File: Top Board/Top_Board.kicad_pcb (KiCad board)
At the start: 2 copper layers, 135.6 x 135.6 mm, 3 parts

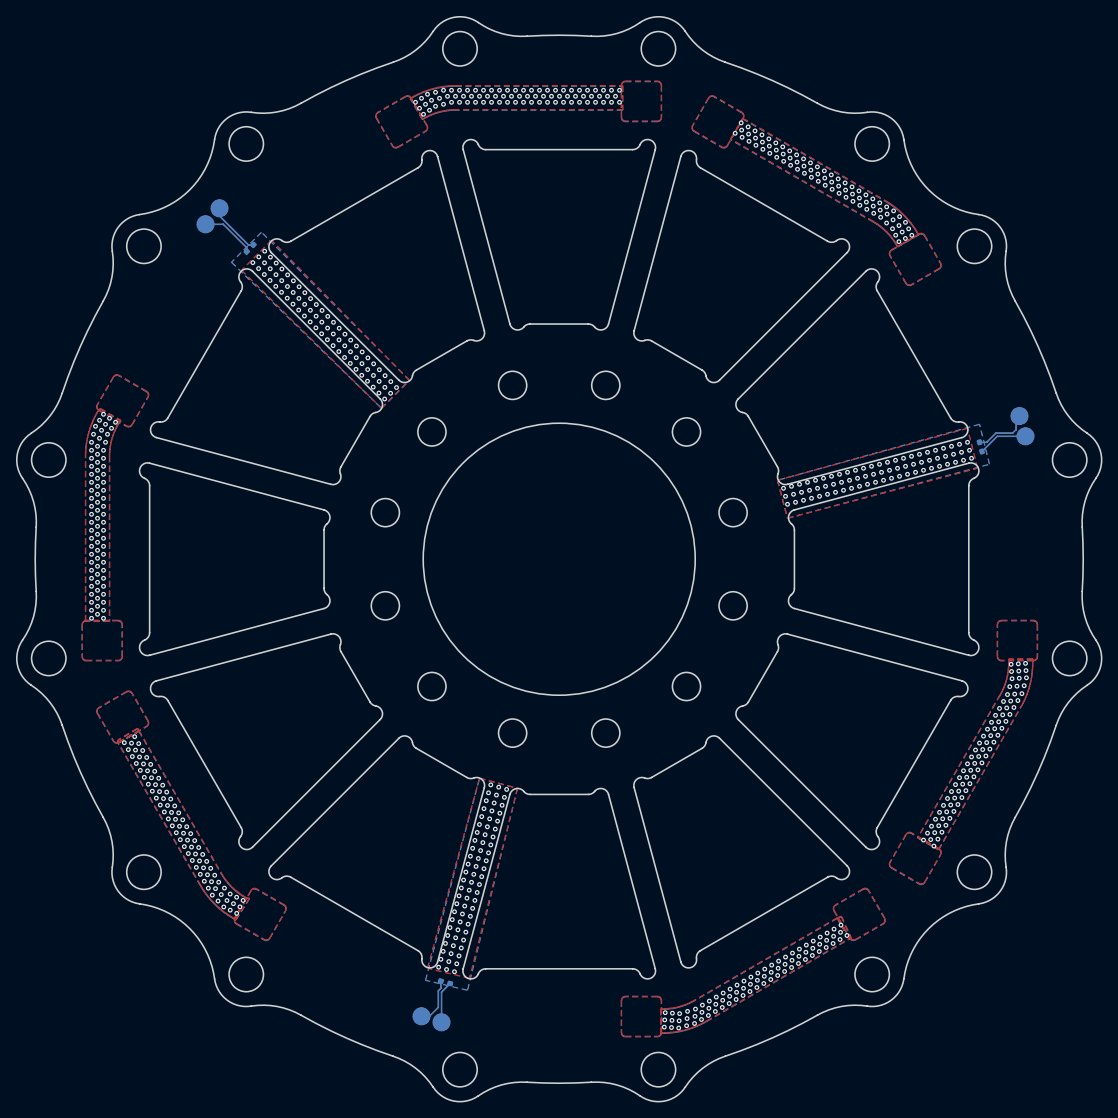
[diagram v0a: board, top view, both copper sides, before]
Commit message: pcbs sent to pcbway
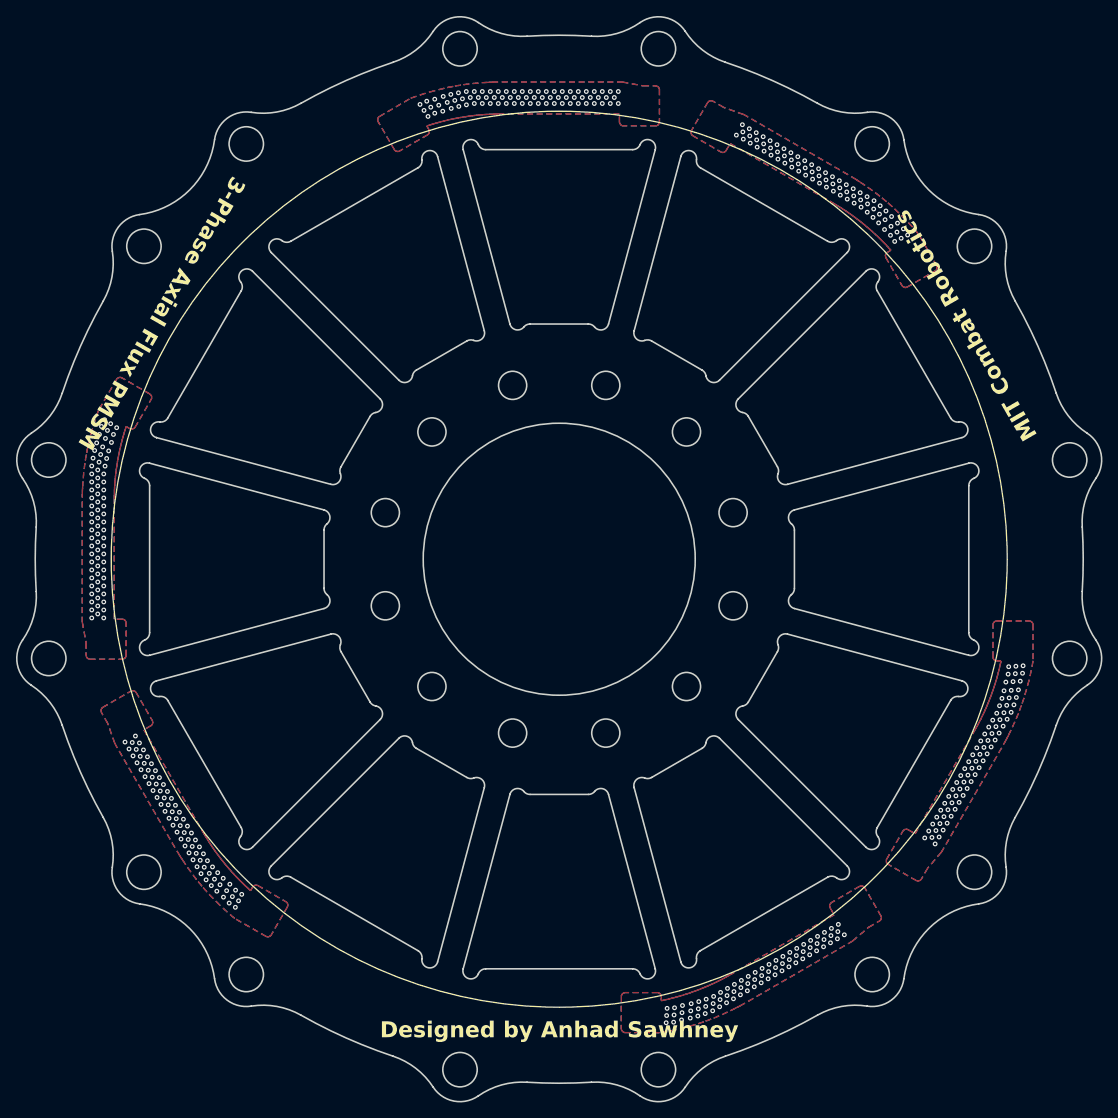
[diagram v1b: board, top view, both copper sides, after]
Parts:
- removed TH1, TH2, TH3: 0402 NTC, Resistor_SMD:R_0402_1005Metric_Pad0.72x0.64mm_HandSolder
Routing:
- net NTC1_B: track 7.11 -> 0.00 mm
- net NTC2_B: track 6.86 -> 0.00 mm
- net NTC2_A: track 6.71 -> 0.00 mm
- net NTC1_A: track 6.23 -> 0.00 mm
- net NTC3_A: track 5.99 -> 0.00 mm
- net NTC3_B: track 5.29 -> 0.00 mm
- net THERM3: vias 72 -> 0
- net THERM2: vias 72 -> 0
- net THERM: vias 72 -> 0
- net BUS6: vias 79 -> 456
- net BUS5: vias 79 -> 0
- net BUS4: vias 79 -> 0
- net BUS3: vias 79 -> 0
- net BUS2: vias 79 -> 0
- net BUS1: vias 79 -> 0
- removed copper zone on B.Cu, net BUS1
- removed copper zone on F.Cu, net BUS1
- removed copper zone on B.Cu, net BUS2
- removed copper zone on F.Cu, net BUS2
- removed copper zone on B.Cu, net BUS3
- removed copper zone on F.Cu, net BUS3
- removed copper zone on B.Cu, net BUS4
- removed copper zone on F.Cu, net BUS4
- removed copper zone on B.Cu, net BUS5
- removed copper zone on F.Cu, net BUS5
- removed copper zone on B.Cu, net THERM
- removed copper zone on F.Cu, net THERM
- removed copper zone on B.Cu, net THERM2
- removed copper zone on F.Cu, net THERM2
- removed copper zone on B.Cu, net THERM3
- removed copper zone on F.Cu, net THERM3
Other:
- outline, holes or cut-outs redrawn
- board text added: "1.6mm"
- board text added: "3-Phase Axial Flux PMSM"
- board text added: "6.72mm"
- board text added: "90°"
- board text added: "A"
- board text added: "BACK side (B.Cu, B.Mask, etc.)"
- board text added: "Countersink on all these holes"
- board text added: "Designed by Anhad Sawhney"
- board text added: "FRONT side (F.Cu, F.Mask, etc.)"
- board text added: "M3 Clearance 6.72mm 90° FRONT SIDE COUNTERSINK"
- board text added: "MIT Combat Robotics"
- board text added: "NO COUNTERSINK on these holes"
- board text added: "Section A"
- board text added: "Section drawing NOT TO SCALE"
